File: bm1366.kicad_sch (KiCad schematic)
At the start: 56 parts, among them J3 Conn_01x05, U1 25MHz, U14 BM1366_mode1, U2 TXB0104RGYR, U5 MCP1824T-1802E, U6 MCP1824T-0802E

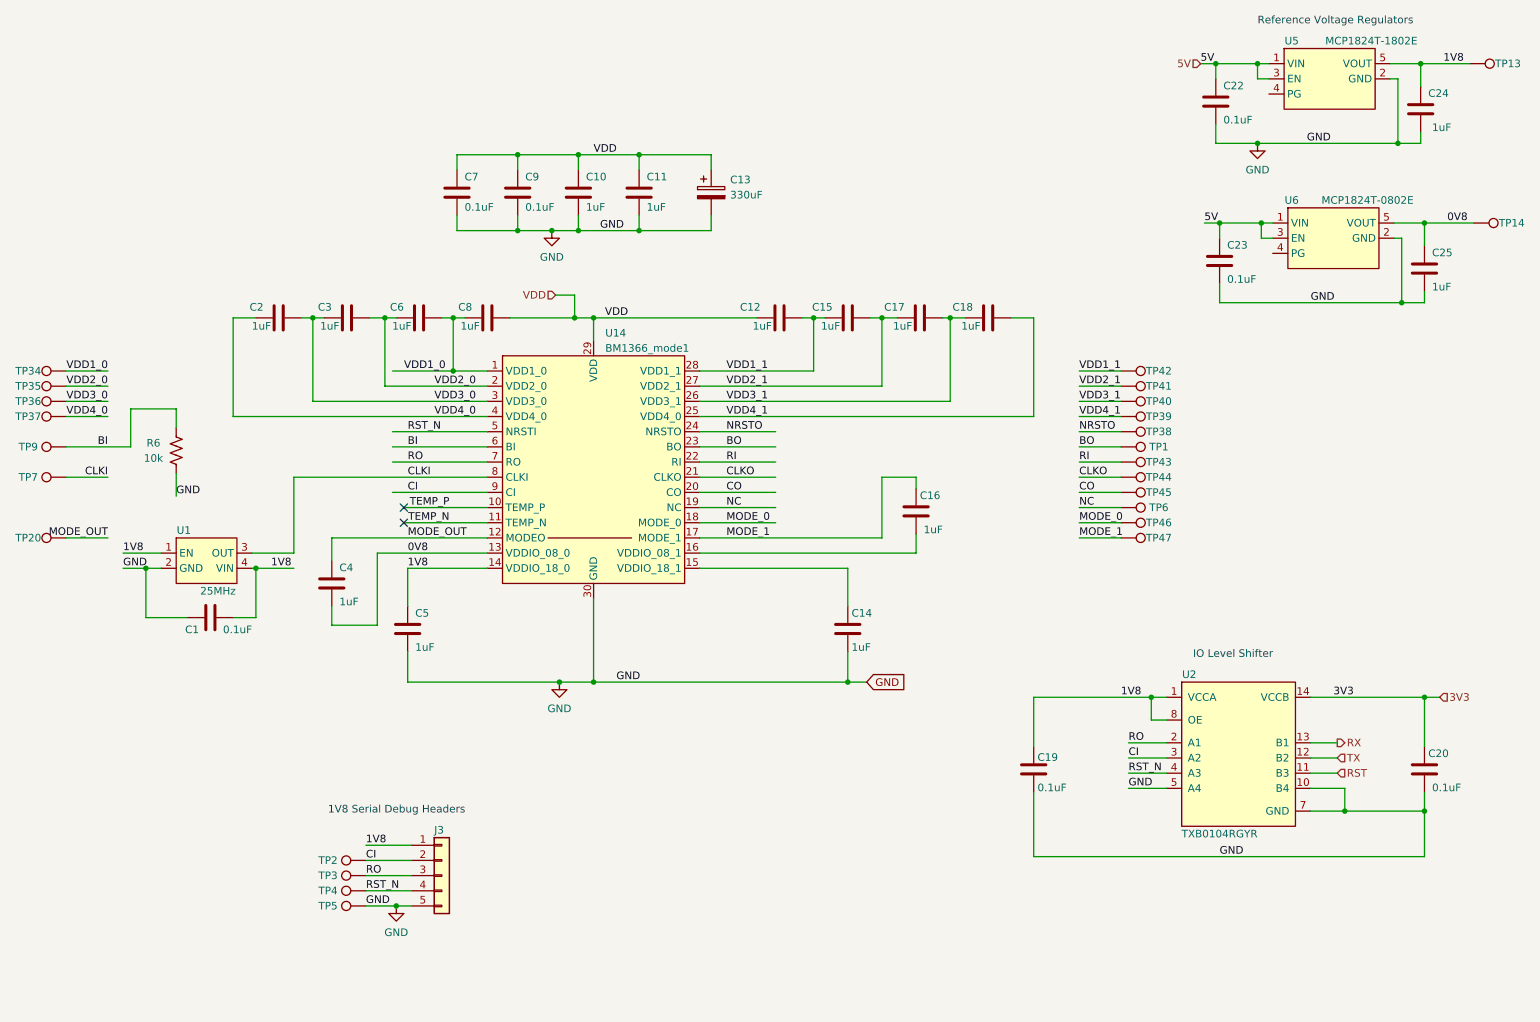
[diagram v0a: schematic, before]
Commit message: added bitaxe variant for rasperry pi
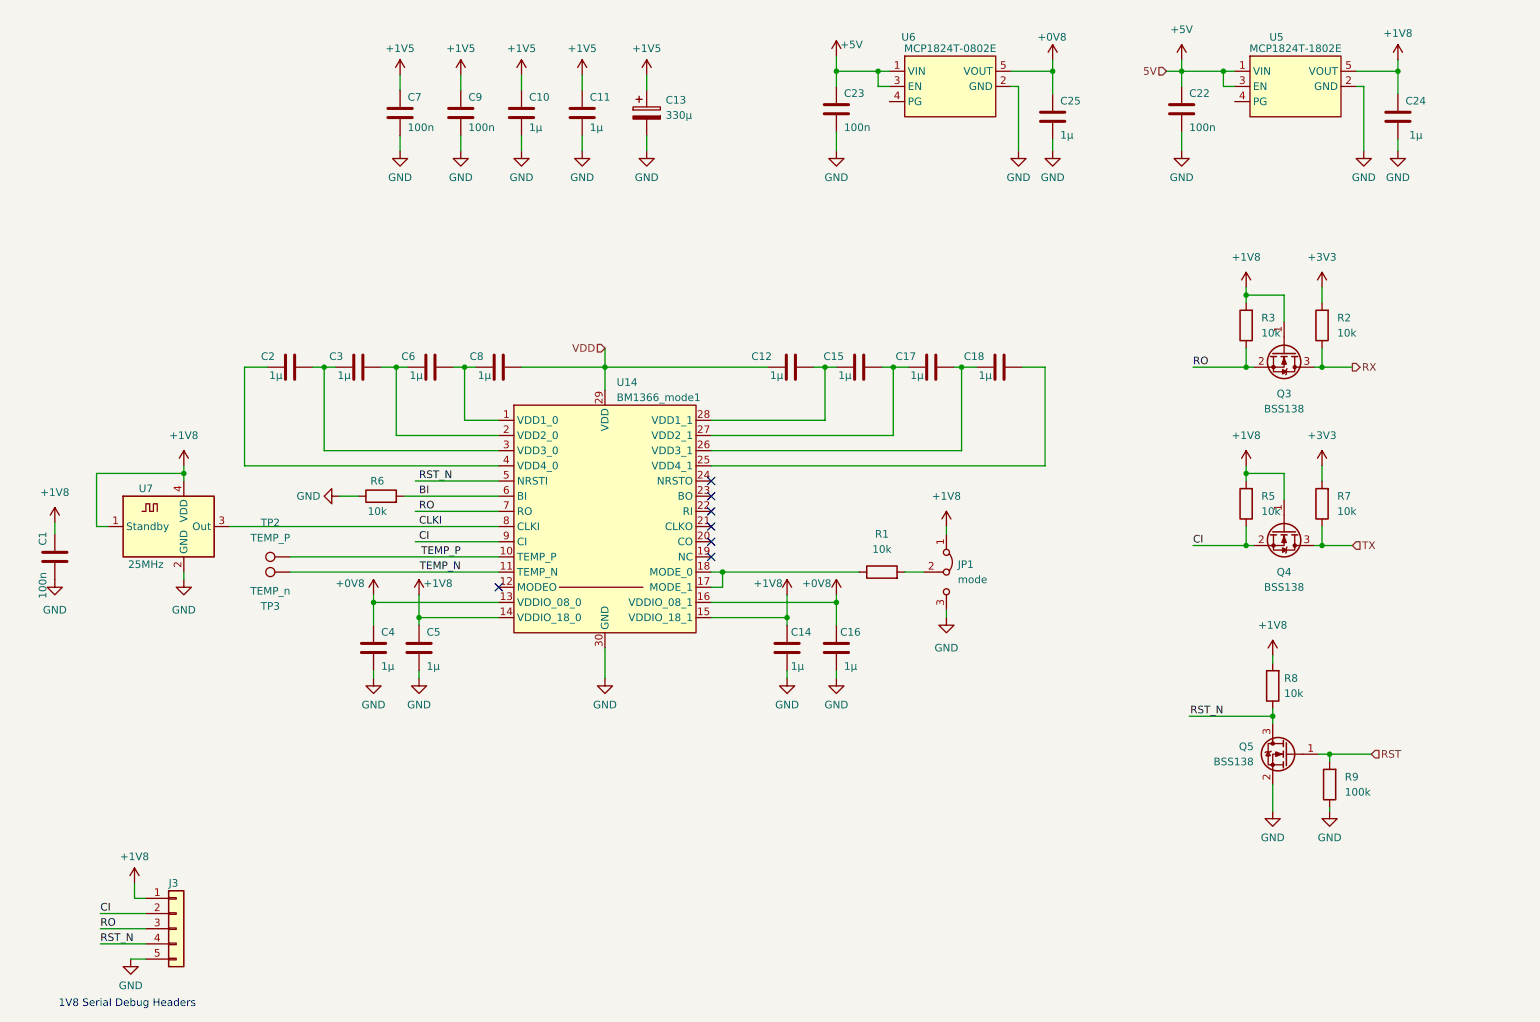
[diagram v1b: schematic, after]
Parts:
- removed C19, C20: 0.1uF, Capacitor_SMD:C_0402_1005Metric, symbol Device:C
- removed R6: 10k, Resistor_SMD:R_0402_1005Metric, symbol Device:R_US
- removed TP1, TP13, TP14, TP20, TP34, TP35, TP36, TP37, TP38, TP39, TP4, TP40, TP41, TP42, TP43, TP44, TP45, TP46, TP47, TP5, TP6, TP7, TP9: TestPoint, TestPoint:TestPoint_Pad_D1.5mm, symbol Connector:TestPoint
- removed U1: 25MHz, bitaxe:O 25,0-JO32-B-1V3-1-T1-LF, symbol bitaxe:oscillator
- removed U2: TXB0104RGYR, bitaxe:TXB0104, symbol bitaxe:TXB0104RGYR
- added JP1: mode, Jumper:SolderJumper-3_P1.3mm_Open_RoundedPad1.0x1.5mm, symbol Jumper:Jumper_3_Bridged12
- added Q3, Q4, Q5: BSS138, Package_TO_SOT_SMD:SOT-23, symbol Transistor_FET:BSS138
- added R1, R2, R3, R5, R6, R7, R8: 10k, Resistor_SMD:R_0805_2012Metric, symbol Device:R
- added R9: 100k, Resistor_SMD:R_0805_2012Metric, symbol Device:R
- added U2, U4, U8: +0V8, symbol mylib7:+0V8
- added U7: 25MHz, Oscillator:Oscillator_SMD_EuroQuartz_XO32-4Pin_3.2x2.5mm, symbol Oscillator:ASDMB-xxxMHz
- C1, C22, C23, C7, C9: value 0.1uF -> 100n; footprint Capacitor_SMD:C_0402_1005Metric -> Capacitor_SMD:C_0805_2012Metric; DK 1292-1639-1-ND -> (none)
- C10, C11, C12, C14, C15, C16, C17, C18, C2, C24, C25, C3, C4, C5, C6, C8: value 1uF -> 1µ; footprint Capacitor_SMD:C_0402_1005Metric -> Capacitor_SMD:C_0805_2012Metric; DK 587-5514-1-ND -> (none)
- C13: value 330uF -> 330µ; DK 718-1028-1-ND -> (none); Distributor (none) -> D; Manufacturer (none) -> 293D337X9010E2TE3; OrderNr (none) -> 718-1028-1-ND
- TP2: value TestPoint -> TEMP_P; footprint TestPoint:TestPoint_Pad_D1.5mm -> TestPoint:TestPoint_Pad_D2.0mm; Distributor (none) -> -; now in the parts list
- TP3: value TestPoint -> TEMP_n; footprint TestPoint:TestPoint_Pad_D1.5mm -> TestPoint:TestPoint_Pad_D2.0mm; Distributor (none) -> -; now in the parts list
- U14: Distributor (none) -> X
- U5: DK MCP1824T-1802E/OTCT-ND -> (none); Distributor (none) -> D; Manufacturer (none) -> MCP1824T-1802E/OT; OrderNr (none) -> MCP1824T-1802E/OTCT-ND; PARTNO MCP1824T-1802E/OT -> (none)
- U6: DK MCP1824T-0802E/OTCT-ND -> (none); Distributor (none) -> D; Manufacturer (none) -> MCP1824T-0802E/OT; OrderNr (none) -> MCP1824T-0802E/OTCT-ND; PARTNO MCP1824T-0802E/OT -> (none)
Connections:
- net BI: now also R6.2
- net CI: now also Q4.2 (S), R5.1; no longer TP2.1
- net CLKI: now also U7.3 (Out)
- net GND: now also C1.2, C16.2, C4.2, JP1.3 (B), Q5.2 (S), R6.1, R9.1, U7.2 (GND); no longer C1.1
- net RO: now also Q3.2 (S), R3.1; no longer TP3.1
- net RST: now also Q5.1 (G), R9.2
- net RST_N: now also Q5.3 (D), R8.1
- net RX: now also Q3.3 (D), R2.1
- net TEMP_N: now also TP3.1
- net TEMP_P: now also TP2.1
- net TX: now also Q4.3 (D), R7.1
- net VDD: no longer C10.1, C11.1, C13.1, C7.1, C9.1
- net +1V8: now reaches C14.1, U14.15 (VDDIO_18_1)
- net +1V8: now also C1.1, C24.1, C5.1, J3.1 (Pin_1), U14.14 (VDDIO_18_0), U5.5 (VOUT), JP1.1 (A), Q3.1 (G), Q4.1 (G), R3.2, R5.2, R8.2, U7.1 (Standby), U7.4 (VDD)
- net +0V8: now reaches U14.16 (VDDIO_08_1)
- net +0V8: now also C16.1, C25.1, C4.1, U14.13 (VDDIO_08_0), U6.5 (VOUT), U2.1 (+0V8), U4.1 (+0V8), U8.1 (+0V8); no longer C16.2
- removed net 0V8: C25.1, C4.2, U14.13 (VDDIO_08_0), U6.5 (VOUT)
- removed net 1V8: C1.2, C24.1, C5.1, J3.1 (Pin_1), U14.14 (VDDIO_18_0), U5.5 (VOUT)
- net 5V renamed +5V
- net BO: no longer names the net of U14.23 (BO)
- net CLKO: no longer names the net of U14.21 (CLKO)
- net CO: no longer names the net of U14.20 (CO)
- net MODE_0: no longer names the net of U14.18 (MODE_0)
- net MODE_0: now also U14.17 (MODE_1), R1.1
- removed net MODE_1: C16.1, U14.17 (MODE_1)
- net MODE_OUT: no longer names the net of U14.12 (MODEO)
- net MODE_OUT: no longer C4.1
- net NC: no longer names the net of U14.19 (NC)
- net NRSTO: no longer names the net of U14.24 (NRSTO)
- net RI: no longer names the net of U14.22 (RI)
- net VDD1_0: no longer names the net of C6.2, C8.1, U14.1 (VDD1_0)
- net VDD1_1: no longer names the net of C12.2, C15.1, U14.28 (VDD1_1)
- net VDD2_0: no longer names the net of C3.2, C6.1, U14.2 (VDD2_0)
- net VDD2_1: no longer names the net of C15.2, C17.1, U14.27 (VDD2_1)
- net VDD3_0: no longer names the net of C2.2, C3.1, U14.3 (VDD3_0)
- net VDD3_1: no longer names the net of C17.2, C18.1, U14.26 (VDD3_1)
- net VDD4_0: no longer names the net of C2.1, U14.4 (VDD4_0)
- net VDD4_1: no longer names the net of C18.2, U14.25 (VDD4_1)
- new net: JP1.2 (C), R1.2
- new net +1V5: C10.1, C11.1, C13.1, C7.1, C9.1
- new net +3V3: R2.2, R7.2
- no-connect marks 2 -> 7
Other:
- note removed: "IO Level Shifter"
- note removed: "Reference Voltage Regulators"
- moved on the sheet: C1, C10, C11, C12, C13, C14, C15, C16, C17, C18, C2, C22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
